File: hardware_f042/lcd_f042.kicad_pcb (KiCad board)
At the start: 2 copper layers, 80 x 50 mm, 120 parts, among them J1 HDMI-A receptacle, J2 USB-C (power + touch USB), J3 AT070TN92 FPC (0.5mm 50P, top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, J4 Touch FPC 6P 0.5mm, J5 SWD/UART, Q1 AO3401A, Q2 2N7002, SW1 BOOT (DFU), U1 LT8619C, U10 STM32F042F6P6, U2 AMS1117-3.3, U3 AMS1117-1.8, U4 USBLC6-2SC6, U7 TPS61040, U8 LM321, U9 TPS61165, Y1 25MHz 12pF

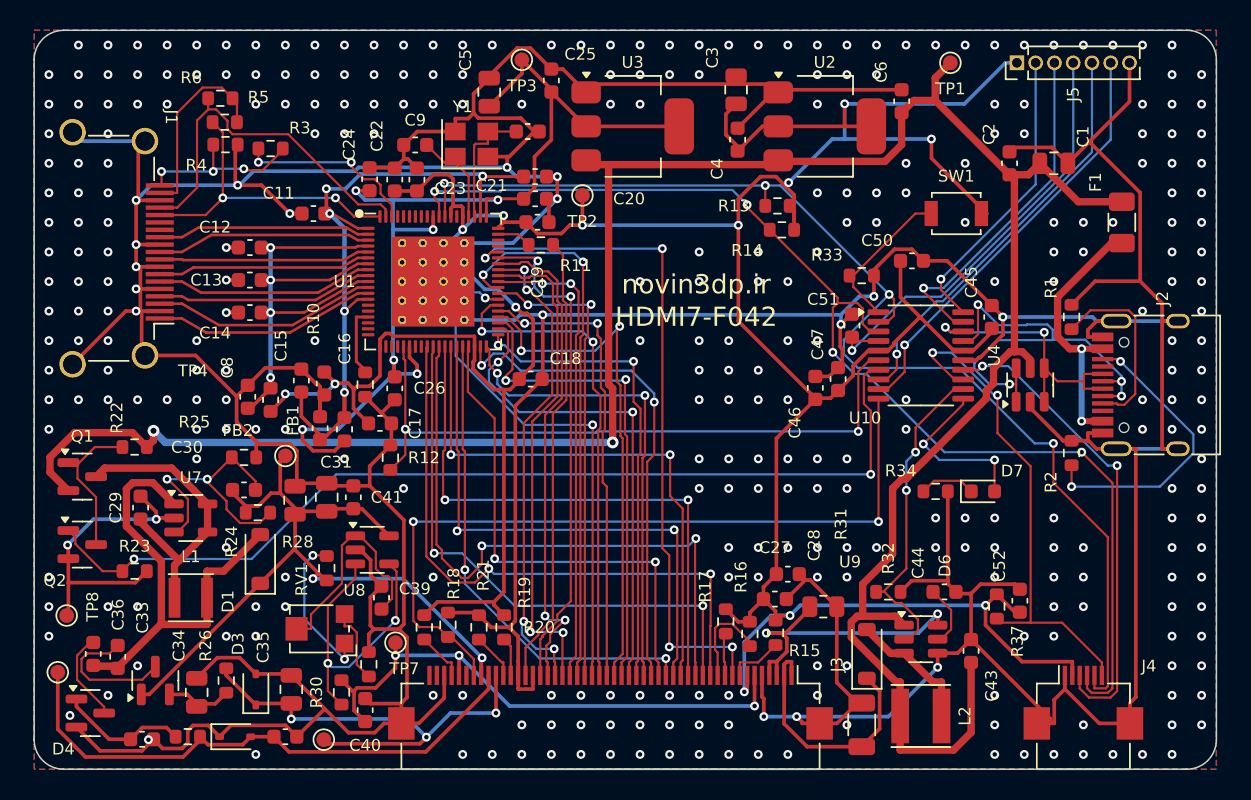
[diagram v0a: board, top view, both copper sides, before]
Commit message: F042 board: move the USB-C next to the HDMI receptacle
The USB-C now sits on the left edge right under the HDMI socket, so
both Raspberry Pi cables leave the board on the same side.

- The USB D+/D-/VBUS pre-routes are rotated with the connector.
- The ESD array U4 moves onto the USB path toward the MCU, since there
  is no room beside the connector.
- The bias switch (Q1/Q2/R22/R23/C29) and TPS61040 (U7, L1) move to
  make room; the parts that had to move are placed last so the rest
  keeps its position.
- Routed copper keeps 0.5 mm from the board edge.

Rerouted: DRC 0 errors, 0 unconnected, netlist matches design.py.

Co-Authored-By: Claude Opus 5.5 <noreply@anthropic.com>
Claude-Session: https://claude.ai/code/session_01X8BrieHZtCS6HfoR48ML9y
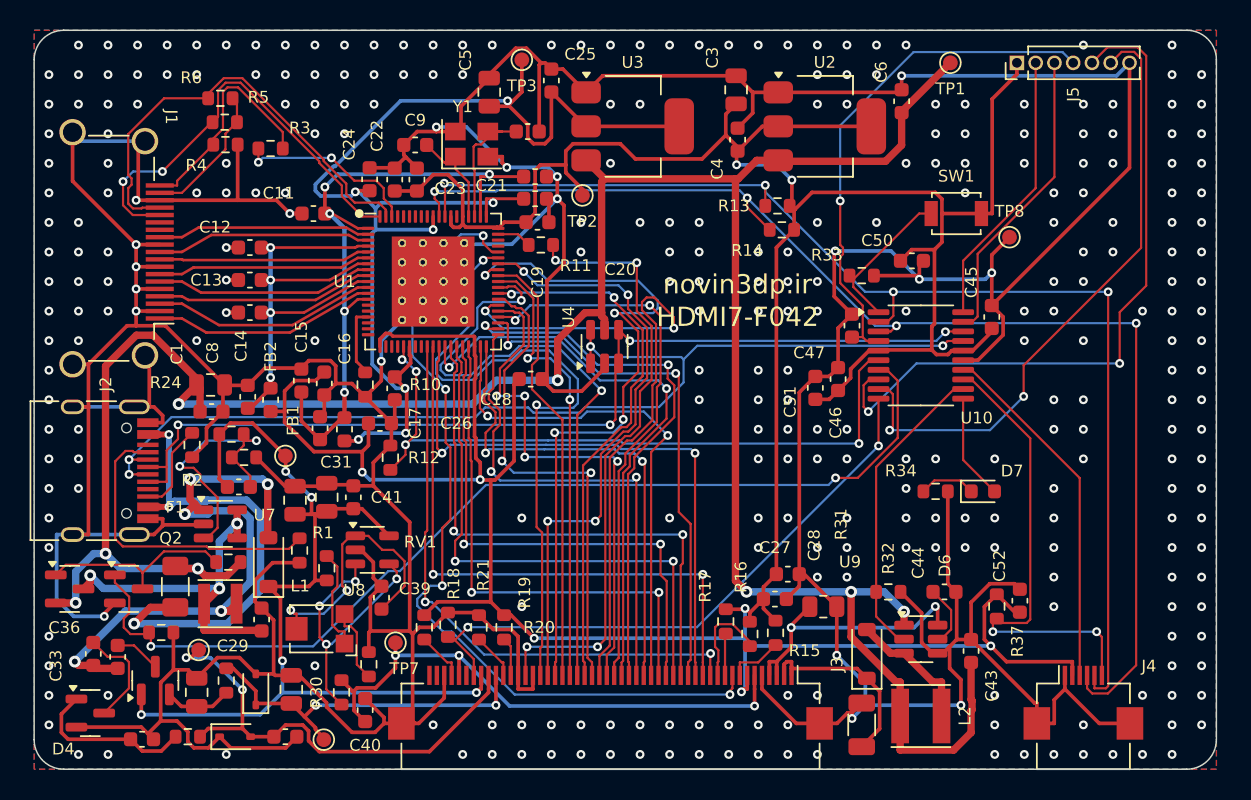
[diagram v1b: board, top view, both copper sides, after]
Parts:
- moved J2 72.9 mm to (103.7, 109.8), turned to -90 degrees
- moved TP8 68.7 mm to (166.0, 94.0)
- moved F1 68.6 mm to (109.6, 117.6)
- moved R2 59.5 mm to (110.7, 108.1), turned to -90 degrees
- moved C1 59.0 mm to (111.9, 104.0)
- moved C2 56.6 mm to (112.0, 105.8), turned to 0 degrees
- moved R1 54.6 mm to (118.0, 115.2), turned to -90 degrees
- moved U4 28.9 mm to (138.6, 101.4)
- moved C29 11.2 mm to (115.4, 119.9)
- moved R22 10.0 mm to (113.1, 116.0)
- moved TP6 9.65 mm to (111.1, 121.9)
- moved Q1 7.65 mm to (102.4, 117.8)
- moved R24 5.60 mm to (113.4, 107.3)
- moved R23 4.52 mm to (108.6, 120.7)
- moved Q2 4.35 mm to (106.4, 117.8)
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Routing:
- net USB_DP: track 19.5 -> 66.5 mm, vias 2 -> 4
- net USB_DM: track 31.1 -> 73.5 mm
- net UART_TX: track 28.0 -> 47.3 mm, vias 1 -> 2
- net +3V3: track 243.9 -> 259.4 mm, vias 13 -> 8
- net LCD_R2: track 32.6 -> 47.8 mm
- net GND: track 555.7 -> 540.7 mm, vias 334 -> 312
- net +1V8: track 71.3 -> 85.5 mm, vias 6 -> 7
- net VBUS: track 18.3 -> 32.4 mm, vias 2 -> 3
- net USB_CC2: track 20.2 -> 6.11 mm, vias 2 -> 0
- net UART_RX: track 29.0 -> 42.3 mm, vias 1 -> 2
- net LCD_DE: track 46.6 -> 58.9 mm
- net AVDD: track 51.5 -> 63.6 mm, vias 2 -> 5
- net LCD_G0: track 33.2 -> 45.3 mm
- net LCD_RST: track 52.8 -> 40.8 mm
- net LCD_DCLK: track 30.6 -> 41.5 mm, vias 0 -> 4
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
